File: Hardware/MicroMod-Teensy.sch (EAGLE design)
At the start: 68 parts, among them J1 MICROMOD-2222, Q1 20V/4.2A/52mΩ/1.4W, Q2 20V/0.2A/8MHz/1.2Ω/1Vth, U1 IMXRT1062DV10X10, U2 W25QXX3X2, U3 MKL02Z32VFG4, Y1 32.768kHz, Y2 24MHz

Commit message: Matches trace lenths to flash. New panel.
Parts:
- TP1: value 32kHz Test -> TEST-POINT2
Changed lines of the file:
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@@
 <part name="FRAME1" library="SparkFun-Aesthetics" deviceset="FRAME-LEDGER" device=""/>
 <part name="U1" library="Teensy" deviceset="IMXRT1062DV" device="10X10"/>
-<part name="TP1" library="SparkFun-Connectors" deviceset="TEST-POINT" device="2" value="32kHz Test"/>
+<part name="TP1" library="SparkFun-Connectors" deviceset="TEST-POINT" device="2" value=""/>
 <part name="D1" library="SparkFun-LED" deviceset="LED-BLUE" device="0603" value="BLUE"/>
 <part name="R1" library="SparkFun-Resistors" deviceset="1KOHM" device="-0402T-1/16W-1%" value="1k"/>
@@
 <part name="GND21" library="SparkFun-PowerSymbols" deviceset="GND" device=""/>
 <part name="GND22" library="SparkFun-PowerSymbols" deviceset="GND" device=""/>
-<part name="TP3" library="SparkFun-Connectors" deviceset="TEST-POINT" device="2" value="TEST-POINT2"/>
+<part name="TP3" library="SparkFun-Connectors" deviceset="TEST-POINT" device="2" value=""/>
 <part name="SUPPLY10" library="SparkFun-PowerSymbols" deviceset="3.3V" device=""/>
 <part name="C14" library="SparkFun-Capacitors" deviceset="4.7UF" device="-0402_TIGHT-6.3V-20%-X5R" value="4.7uF"/>
@@
 <part name="C22" library="SparkFun-Capacitors" deviceset="0.22UF" device="-0402T-10V-10%" value="0.22uF"/>
 <part name="GND35" library="SparkFun-PowerSymbols" deviceset="GND" device=""/>
-<part name="TP4" library="SparkFun-Connectors" deviceset="TEST-POINT" device="2" value="TEST-POINT2"/>
+<part name="TP4" library="SparkFun-Connectors" deviceset="TEST-POINT" device="2" value=""/>
 <part name="SUPPLY16" library="SparkFun-PowerSymbols" deviceset="V_BATT" device=""/>
 <part name="SUPPLY17" library="SparkFun-PowerSymbols" deviceset="3.3V" device=""/>
@@
 <part name="C27" library="SparkFun-Capacitors" deviceset="4.7UF" device="-0402_TIGHT-6.3V-20%-X5R" value="4.7uF"/>
 <part name="GND40" library="SparkFun-PowerSymbols" deviceset="GND" device=""/>
-<part name="TP5" library="SparkFun-Connectors" deviceset="TEST-POINT" device="2" value="TEST-POINT2"/>
-<part name="TP6" library="SparkFun-Connectors" deviceset="TEST-POINT" device="2" value="TEST-POINT2"/>
-<part name="TP7" library="SparkFun-Connectors" deviceset="TEST-POINT" device="2" value="TEST-POINT2"/>
+<part name="TP5" library="SparkFun-Connectors" deviceset="TEST-POINT" device="2" value=""/>
+<part name="TP6" library="SparkFun-Connectors" deviceset="TEST-POINT" device="2" value=""/>
+<part name="TP7" library="SparkFun-Connectors" deviceset="TEST-POINT" device="2" value=""/>
 <part name="FD1" library="SparkFun-Aesthetics" deviceset="FIDUCIAL" device="UFIDUCIAL"/>
 <part name="FD2" library="SparkFun-Aesthetics" deviceset="FIDUCIAL" device="UFIDUCIAL"/>
@@
 <part name="D5" library="SparkFun-LED" deviceset="LED-YELLOW" device="0603" value="Yellow"/>
 <part name="SUPPLY19" library="SparkFun-PowerSymbols" deviceset="3.3V" device=""/>
-<part name="TP8" library="SparkFun-Connectors" deviceset="TEST-POINT" device="2" value="TEST-POINT2"/>
-<part name="TP9" library="SparkFun-Connectors" deviceset="TEST-POINT" device="2" value="TEST-POINT2"/>
+<part name="TP8" library="SparkFun-Connectors" deviceset="TEST-POINT" device="2" value=""/>
+<part name="TP9" library="SparkFun-Connectors" deviceset="TEST-POINT" device="2" value=""/>
 <part name="C28" library="SparkFun-Capacitors" deviceset="0.22UF" device="-0402T-10V-10%" value="0.22uF"/>
 <part name="SUPPLY20" library="SparkFun-PowerSymbols" deviceset="3.3V" device=""/>
 <part name="GND43" library="SparkFun-PowerSymbols" deviceset="GND" device=""/>
-<part name="TP10" library="SparkFun-Connectors" deviceset="TEST-POINT" device="2" value="TEST-POINT2"/>
-<part name="TP11" library="SparkFun-Connectors" deviceset="TEST-POINT" device="2" value="TEST-POINT2"/>
+<part name="TP10" library="SparkFun-Connectors" deviceset="TEST-POINT" device="2" value=""/>
+<part name="TP11" library="SparkFun-Connectors" deviceset="TEST-POINT" device="2" value=""/>
 <part name="SUPPLY6" library="SparkFun-PowerSymbols" deviceset="3.3V" device=""/>
 <part name="GND8" library="SparkFun-PowerSymbols" deviceset="GND" device=""/>
 <part name="L2" library="SparkFun-Coils" deviceset="4.7μH_SHIELDED_INDUCTOR" device="" value="4.7μH"/>
 <part name="J1" library="Teensy" deviceset="MICROMOD" device="-2222"/>
-<part name="TP2" library="SparkFun-Connectors" deviceset="TEST-POINT" device="2" value="TEST-POINT2"/>
+<part name="TP2" library="SparkFun-Connectors" deviceset="TEST-POINT" device="2" value=""/>
 <part name="Q1" library="SparkFun-DiscreteSemi" deviceset="MOSFET_PCH" device="-DMG2305UX-7" value="20V/4.2A/52mΩ/1.4W"/>
 <part name="Q2" library="SparkFun-DiscreteSemi" deviceset="MOSFET-NCH" device="-RE1C00UNTL" value="20V/0.2A/8MHz/1.2Ω/1Vth"/>

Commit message: Route bus pins to v11.
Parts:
- added LOGO2: OSHW-LOGONO_SILK, SparkFun-Aesthetics:OSHW-LOGONO_SILK
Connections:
- new net GPIO/40: J1.G0/BUS0, U1.B0_04
- new net GPIO/41: J1.G1/BUS1, U1.B0_05
- new net GPIO/42: J1.G2/BUS2, U1.B0_06
- new net GPIO/43: J1.G3/BUS3, U1.B0_07
- new net GPIO/44: J1.G4/BUS4, U1.B0_08
- new net GPIO/45: J1.G5/BUS5, U1.B0_09
- net AUD_IN/8: now also J1.AUD_IN/CAM_PCLK; no longer J1.AUD_IN
- net AUD_OUT/7: now also J1.AUD_OUT/CAM_MCLK; no longer J1.AUD_OUT
- net D1/5: now also J1.D1/CAM_TRIG; no longer J1.D1
- net GPIO/26/A12: now also J1.G8; no longer J1.G1
- net GPIO/27/A13: now also J1.G11; no longer J1.G2
- net GPIO/28: no longer J1.G3
- net GPIO/32: now also J1.G9/ADC_D-/CAM_HSYNC; no longer J1.G4
- net GPIO/33: now also J1.G10/ADC_D+/CAM_VSYNC; no longer J1.G5
- net GPIO/6: now also J1.G6/BUS6; no longer J1.G0
- net GPIO/9: now also J1.G7/BUS7; no longer J1.G6
- net MCLK/23/A9: now also J1.AUD_MCLK; no longer J1.AUD_MCLK/CLKOUT
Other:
- note added: "Flex2 B0_04"
- note added: "Flex2 B0_05"
- note added: "Flex2 B0_06"
- note added: "Flex2 B0_07"
- note added: "Flex2 B0_08"
- note added: "Flex2 B0_09"
- note added: "Flex2 B0_10"
- note added: "Flex2 B0_11"
- note added: "Flex2 B0_12"
- note added: "Flex2 B1_00"
- note added: "Flex2 B1_01"
- note added: "N. Seidle"
- note added: "Not Flex"
- note added: "v11"
- moved on the sheet: C1, C10, C11, C12, C13, C14, C15, C16, C17, C18, C19, C2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

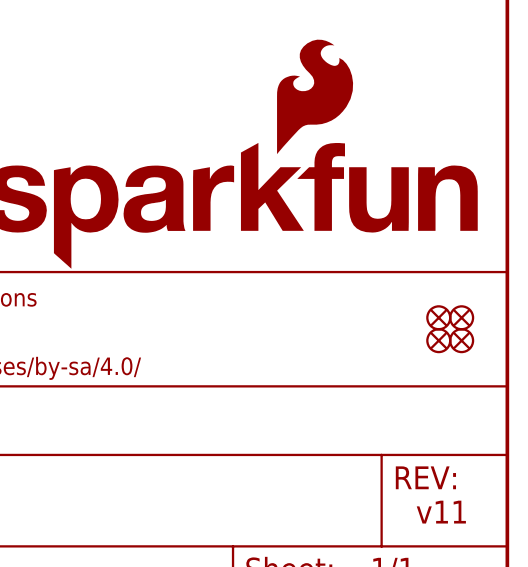
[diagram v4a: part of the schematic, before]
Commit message: Add ordering instructions
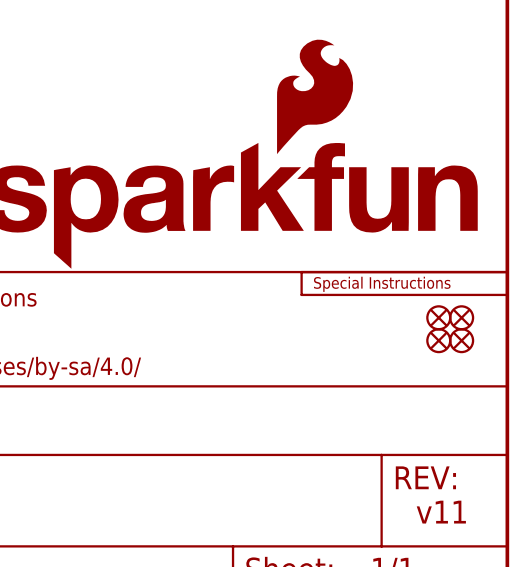
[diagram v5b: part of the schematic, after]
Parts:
- added LOGO3: SPECIAL_INSTRUCTIONS-ORDERING, SparkFun-Aesthetics:SPECIAL_INSTRUCTIONS-ORDERING
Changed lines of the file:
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@@
 <?xml version="1.0" encoding="utf-8"?>
 <!DOCTYPE eagle SYSTEM "eagle.dtd">
-<eagle version="9.5.2">
+<eagle version="9.6.0">
 <drawing>
 <settings>
@@
 <part name="SUPPLY1" library="SparkFun-PowerSymbols" deviceset="3.3V" device=""/>
 <part name="LOGO2" library="SparkFun-Aesthetics" deviceset="OSHW-LOGO" device="NO_SILK"/>
+<part name="LOGO3" library="SparkFun-Aesthetics" deviceset="SPECIAL_INSTRUCTIONS" device="-ORDERING"/>
 </parts>
 <sheets>
@@
 </instance>
 <instance part="LOGO2" gate="G$1" x="358.14" y="45.72" smashed="yes"/>
+<instance part="LOGO3" gate="G$1" x="408.94" y="33.02" smashed="yes"/>
 </instances>
 <busses>

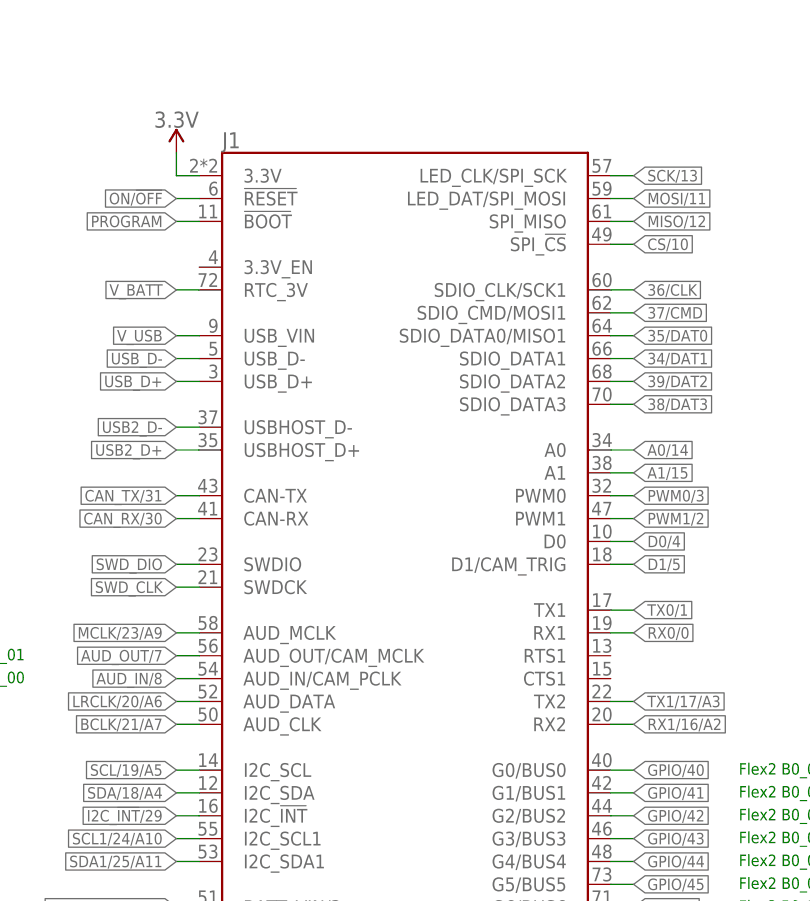
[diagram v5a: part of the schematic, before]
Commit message: Update Micromod connector to current version
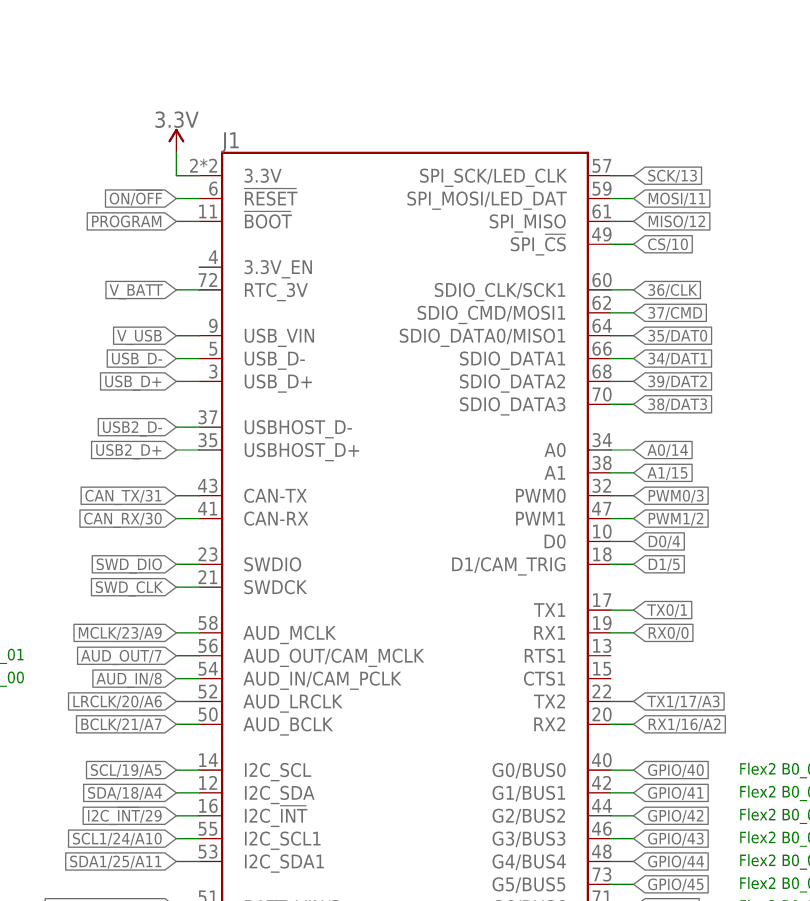
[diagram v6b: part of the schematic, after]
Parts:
- J1: device Teensy:MICROMOD-2222 -> SparkFun-MicroMod:MICROMOD-2222
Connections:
- net BCLK/21/A7: now also J1.AUD_BCLK; no longer J1.AUD_CLK
- net LRCLK/20/A6: now also J1.AUD_LRCLK; no longer J1.AUD_DATA
- net MOSI/11: now also J1.SPI_MOSI/LED_DAT; no longer J1.LED_DAT/SPI_MOSI
- net SCK/13: now also J1.SPI_SCK/LED_CLK; no longer J1.LED_CLK/SPI_SCK
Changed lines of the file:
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@@
 <part name="GND8" library="SparkFun-PowerSymbols" deviceset="GND" device=""/>
 <part name="L2" library="SparkFun-Coils" deviceset="4.7μH_SHIELDED_INDUCTOR" device="" value="4.7μH"/>
-<part name="J1" library="Teensy" deviceset="MICROMOD" device="-2222"/>
+<part name="J1" library="SparkFun-MicroMod" deviceset="MICROMOD" device="-2222"/>
 <part name="TP2" library="SparkFun-Connectors" deviceset="TEST-POINT" device="2" value=""/>
 <part name="Q1" library="SparkFun-DiscreteSemi" deviceset="MOSFET_PCH" device="-DMG2305UX-7" value="20V/4.2A/52mΩ/1.4W"/>
@@
 <wire x1="347.98" y1="177.8" x2="350.52" y2="177.8" width="0.1524" layer="91"/>
 <label x="350.52" y="177.8" size="1.27" layer="95" rot="MR180" xref="yes"/>
-<pinref part="J1" gate="J1" pin="LED_CLK/SPI_SCK"/>
+<pinref part="J1" gate="J1" pin="SPI_SCK/LED_CLK"/>
 </segment>
 </net>
@@
 <wire x1="347.98" y1="175.26" x2="350.52" y2="175.26" width="0.1524" layer="91"/>
 <label x="350.52" y="175.26" size="1.27" layer="95" rot="MR180" xref="yes"/>
-<pinref part="J1" gate="J1" pin="LED_DAT/SPI_MOSI"/>
+<pinref part="J1" gate="J1" pin="SPI_MOSI/LED_DAT"/>
 </segment>
 </net>
@@
 <wire x1="302.26" y1="119.38" x2="299.72" y2="119.38" width="0.1524" layer="91"/>
 <label x="299.72" y="119.38" size="1.27" layer="95" rot="R180" xref="yes"/>
-<pinref part="J1" gate="J1" pin="AUD_DATA"/>
+<pinref part="J1" gate="J1" pin="AUD_LRCLK"/>
 </segment>
 <segment>
@@
 <wire x1="302.26" y1="116.84" x2="299.72" y2="116.84" width="0.1524" layer="91"/>
 <label x="299.72" y="116.84" size="1.27" layer="95" rot="R180" xref="yes"/>
-<pinref part="J1" gate="J1" pin="AUD_CLK"/>
-</segment>
-<segment>
+<pinref part="J1" gate="J1" pin="AUD_BCLK"/>
+</segment>
+<segment>

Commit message: Adding test point measurements
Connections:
- net N$1 renamed TP1
- net N$30 renamed TP5
- net N$33 renamed TP6
- net N$34 renamed TP7
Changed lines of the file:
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@@
 </segment>
 </net>
-<net name="N$1" class="0">
+<net name="TP1" class="0">
 <segment>
 <pinref part="U1" gate="U1" pin="AD_B0_00"/>
@@
 </segment>
 </net>
-<net name="N$30" class="0">
+<net name="TP5" class="0">
 <segment>
 <pinref part="U1" gate="U1" pin="VDD_SNVS_CAP"/>
@@
 </segment>
 </net>
-<net name="N$33" class="0">
+<net name="TP6" class="0">
 <segment>
 <pinref part="U1" gate="U1" pin="NVCC_PLL"/>
@@
 </segment>
 </net>
-<net name="N$34" class="0">
+<net name="TP7" class="0">
 <segment>
 <pinref part="U1" gate="U1" pin="VDD_HIGH_CAP"/>

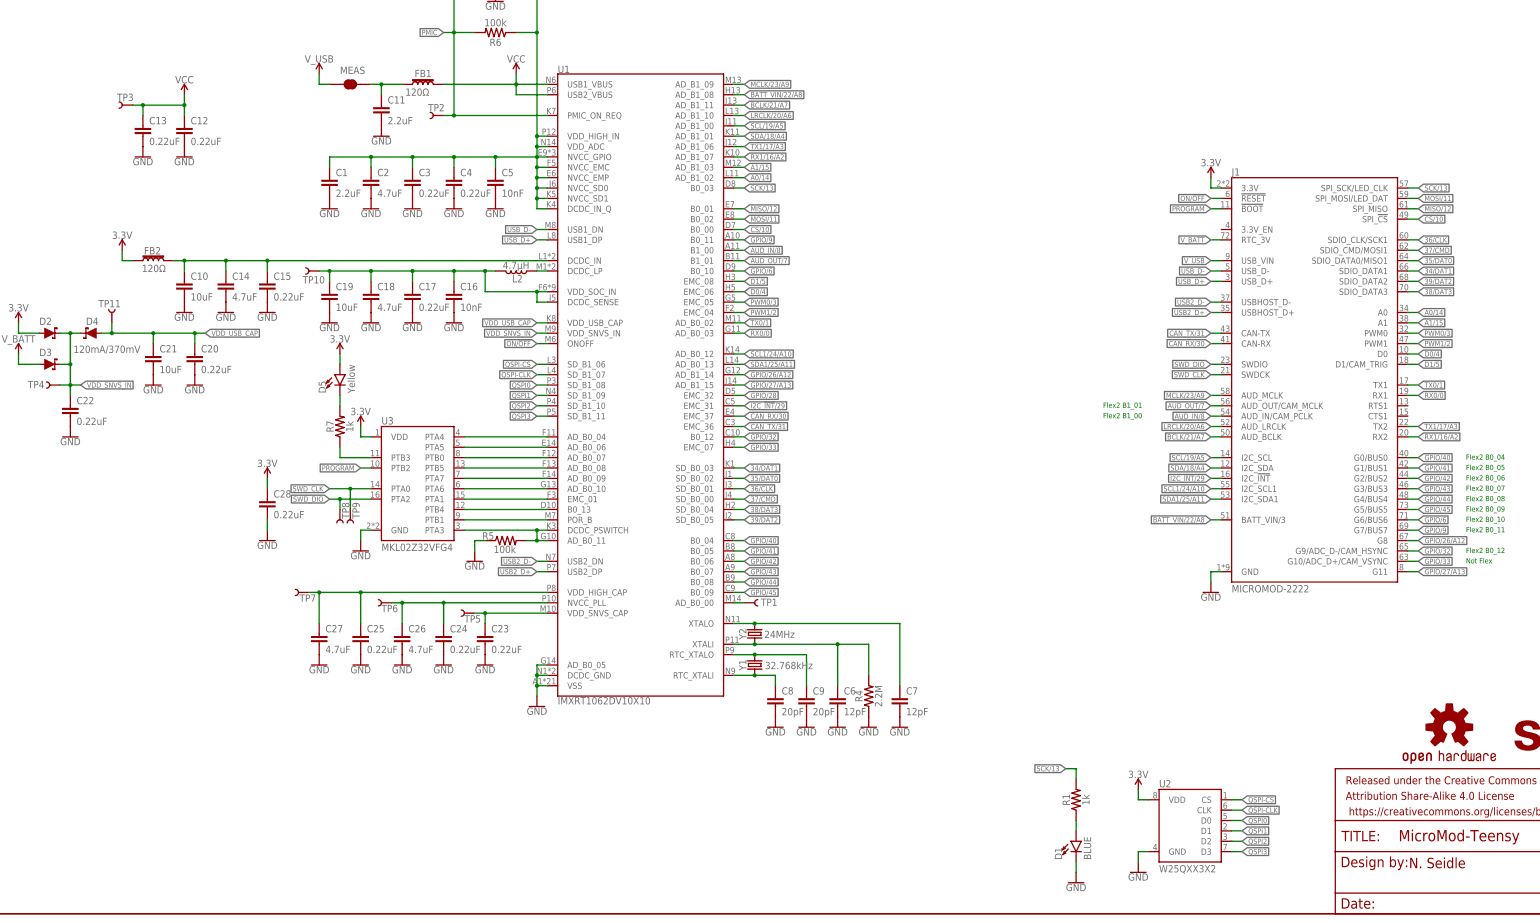
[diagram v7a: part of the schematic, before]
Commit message: Add 3.3V EN. Increase flash IC size to 6x5mm.
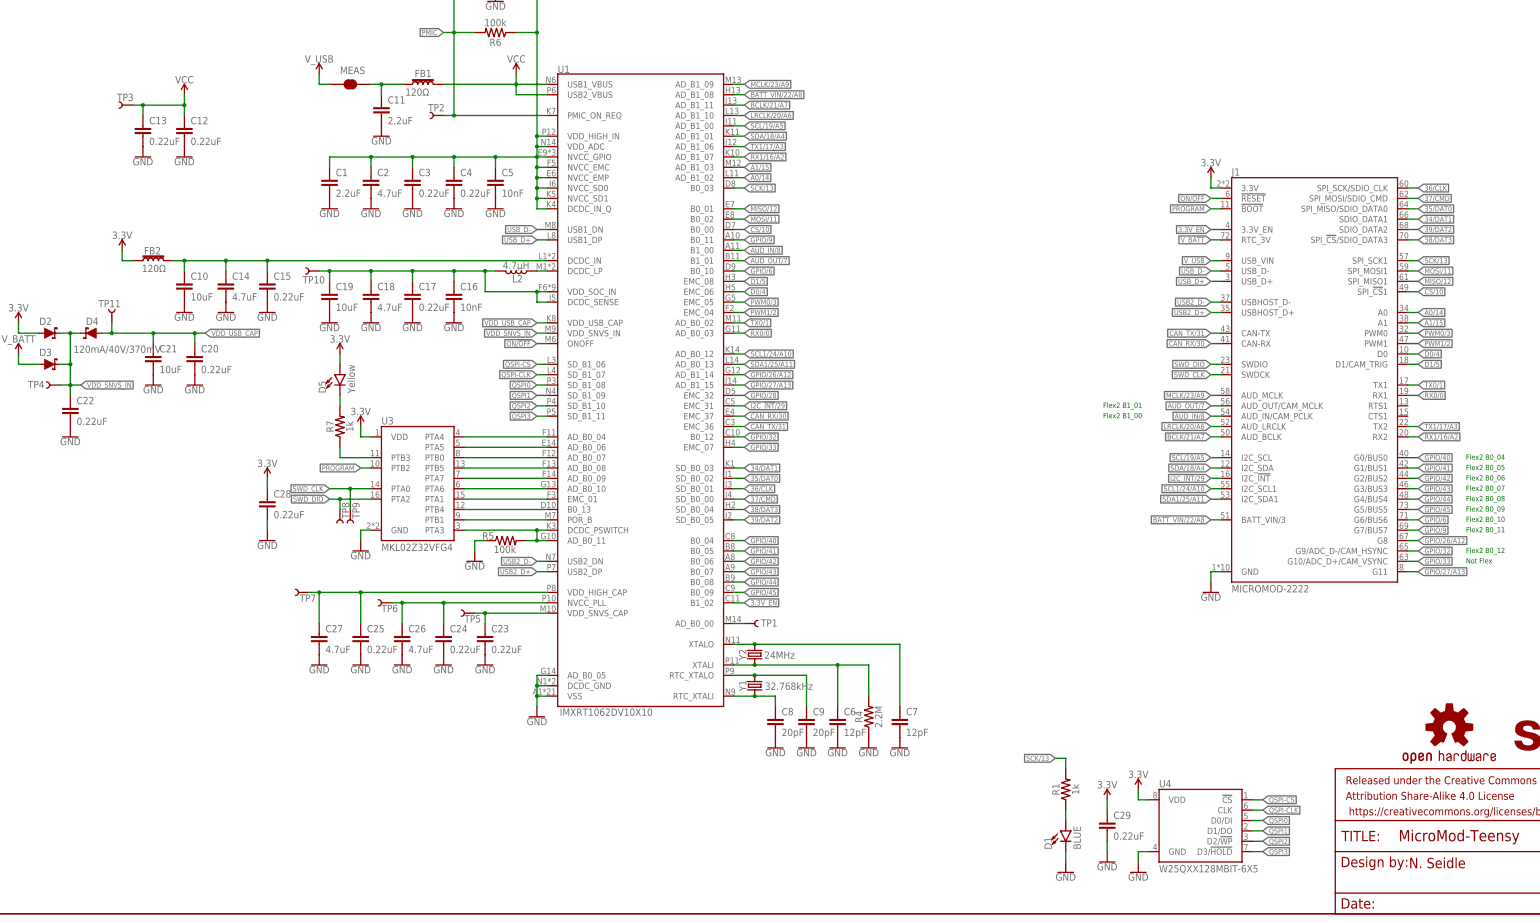
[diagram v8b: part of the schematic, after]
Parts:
- removed U2: W25QXX3X2, Teensy:W25QXX3X2
- added C29: 0.22uF, SparkFun-Capacitors:0.22UF-0402T-10V-10%
- added U4: W25QXX128MBIT-6X5, SparkFun-MicroMod:W25QXX128MBIT-6X5-SKINNY_CENTER
- D2: value 120mA370mV -> 120mA/40V/370mV
- D3, D4: value 120mA/370mV -> 120mA/40V/370mV
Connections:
- new net 3.3V_EN: J1.3.3V_EN, U1.B1_02
- net 3.3V: now also C29.1, U4.VDD; no longer U2.VDD
- net 35/DAT0: now also J1.SPI_MISO/SDIO_DATA0; no longer J1.SDIO_DATA0/MISO1
- net 36/CLK: now also J1.SPI_SCK/SDIO_CLK; no longer J1.SDIO_CLK/SCK1
- net 37/CMD: now also J1.SPI_MOSI/SDIO_CMD; no longer J1.SDIO_CMD/MOSI1
- net 38/DAT3: now also J1.SPI_!CS!/SDIO_DATA3; no longer J1.SDIO_DATA3
- net CS/10: now also J1.SPI_!CS!1; no longer J1.SPI_!CS!
- net GND: now also C29.2, U4.GND; no longer U2.GND
- net MISO/12: now also J1.SPI_MISO1; no longer J1.SPI_MISO
- net MOSI/11: now also J1.SPI_MOSI1; no longer J1.SPI_MOSI/LED_DAT
- net QSPI-CLK: now also U4.CLK; no longer U2.CLK
- net QSPI-CS: now also U4.!CS!; no longer U2.CS
- net QSPI0: now also U4.D0/DI; no longer U2.D0
- net QSPI1: now also U4.D1/DO; no longer U2.D1
- net QSPI2: now also U4.D2/!WP!; no longer U2.D2
- net QSPI3: now also U4.D3/!HOLD!; no longer U2.D3
- net SCK/13: now also J1.SPI_SCK1; no longer J1.SPI_SCK/LED_CLK
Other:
- moved on the sheet: C6, C7, C8, C9, D1, J1, R1, R4, TP1, Y1, Y2
